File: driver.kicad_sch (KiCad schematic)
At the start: 39 parts, among them Q4 SIZ342ADT, Q5 SIZ342ADT, Q6 SIZ342ADT, U4 TMC6200

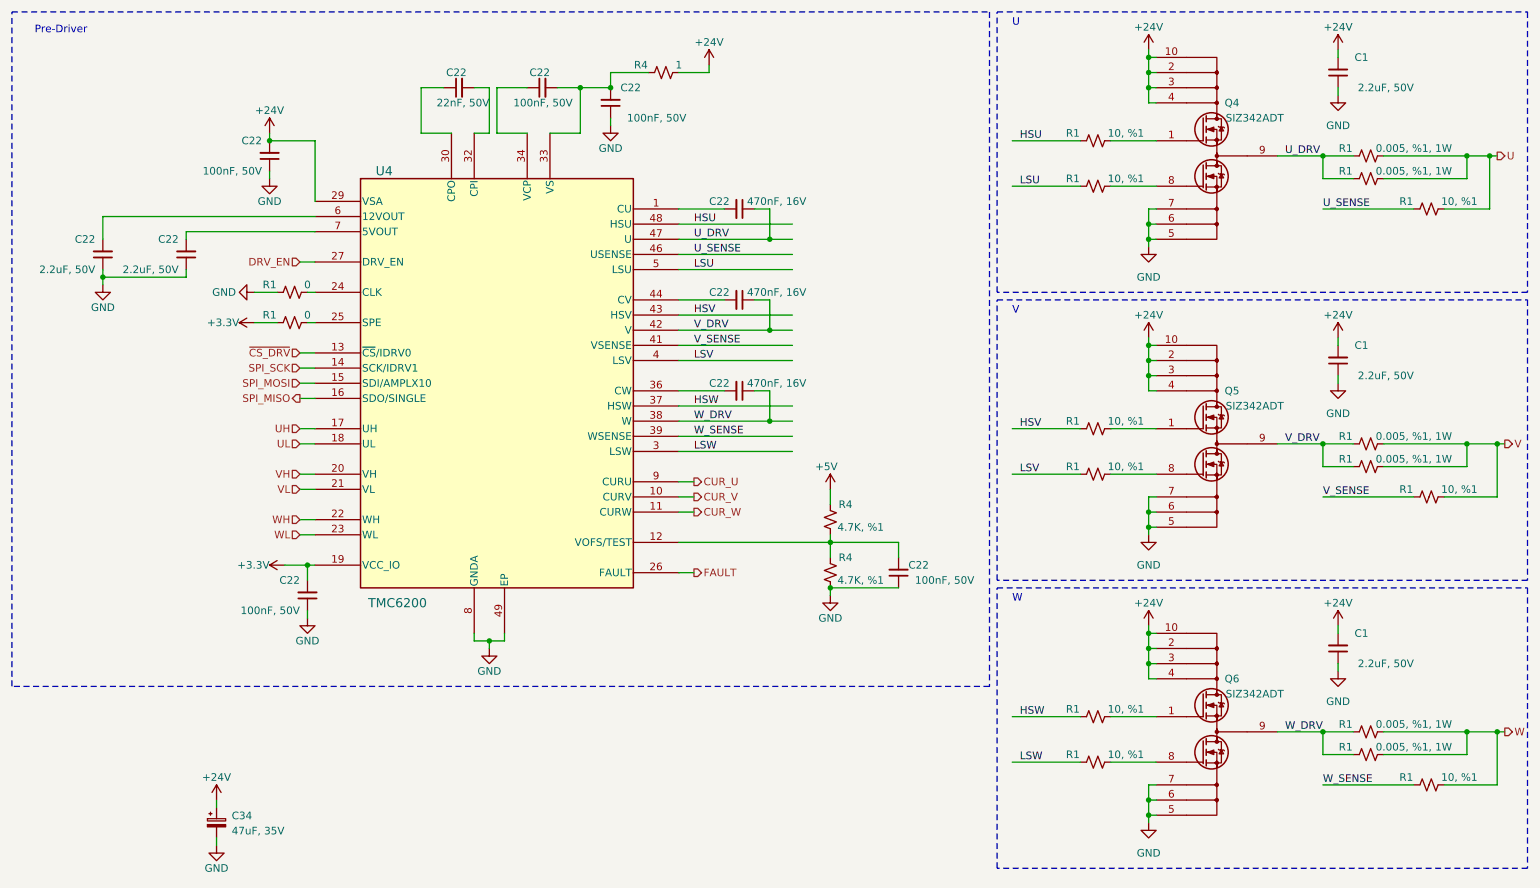
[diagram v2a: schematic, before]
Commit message: Optimize the BOM.
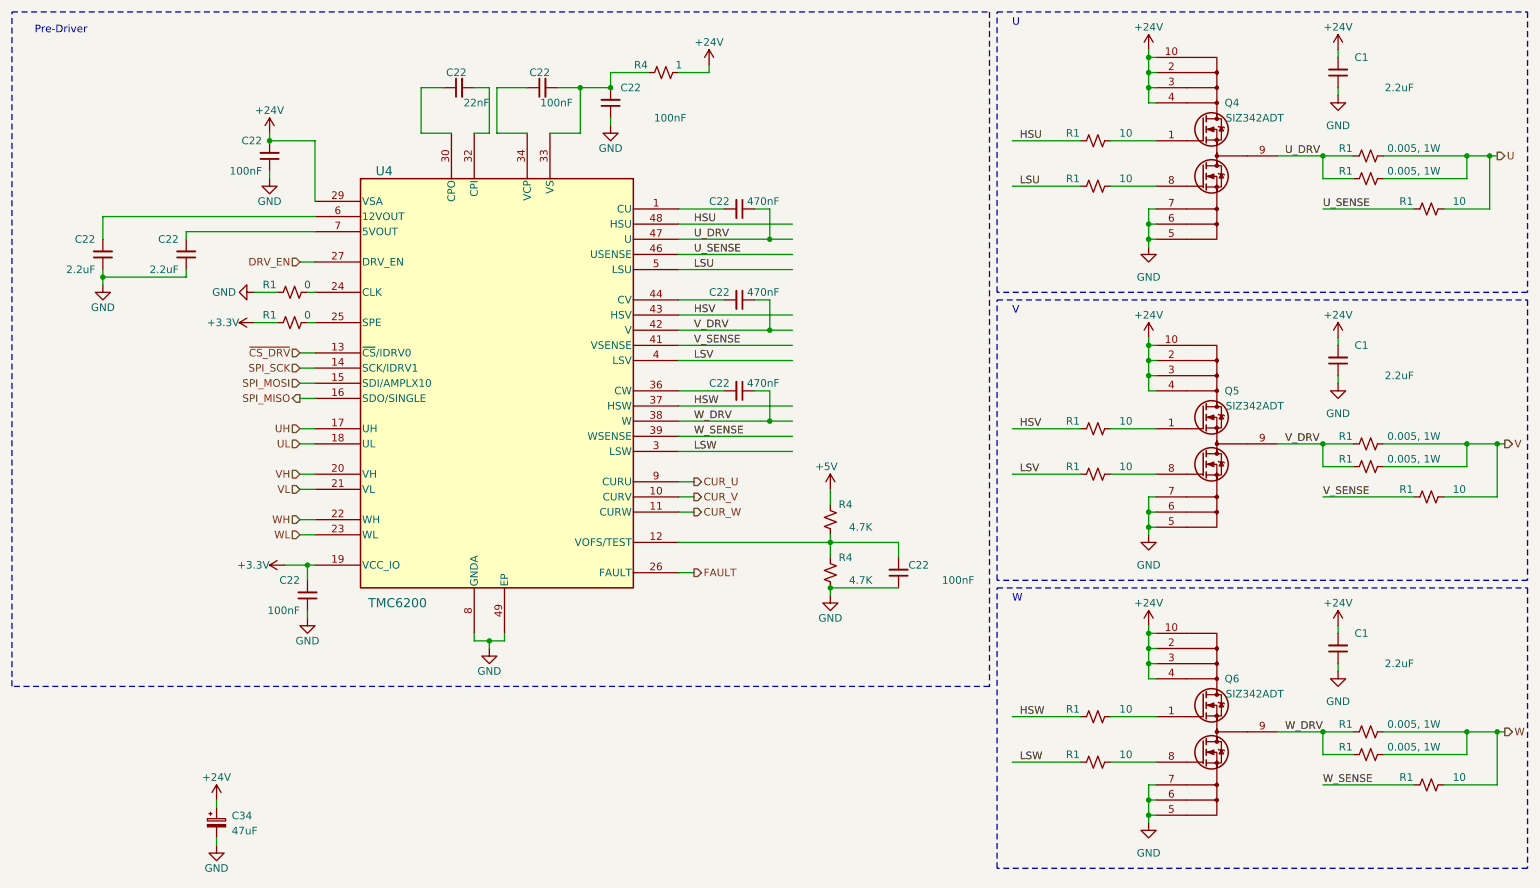
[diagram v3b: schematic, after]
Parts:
- C1, C22: value 2.2uF, 50V -> 2.2uF
- C22: value 100nF, 50V -> 100nF
- C22: value 22nF, 50V -> 22nF
- C22: value 470nF, 16V -> 470nF; MPN C0603C474K4RAC7867 -> GRM188R71E474KA12J
- C34: value 47uF, 35V -> 47uF
- R1: value 10, %1 -> 10
- R1: value 0.005, %1, 1W -> 0.005, 1W
- R4: value 4.7K, %1 -> 4.7K
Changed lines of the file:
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@@
       (effects (font (size 1.27 1.27)))
     )
-    (property "Value" "10, %1" (at 204.47 43.18 90)
+    (property "Value" "10" (at 204.47 43.18 90)
       (effects (font (size 1.27 1.27)))
     )
@@
       (effects (font (size 1.27 1.27)) (justify left))
     )
-    (property "Value" "100nF, 50V" (at 59.69 41.91 0)
+    (property "Value" "100nF" (at 59.69 41.91 0)
       (effects (font (size 1.27 1.27)) (justify left))
     )
@@
       (effects (font (size 1.27 1.27)) (justify left))
     )
-    (property "Value" "2.2uF, 50V" (at 31.75 58.42 0)
+    (property "Value" "2.2uF" (at 31.75 58.42 0)
       (effects (font (size 1.27 1.27)) (justify left))
     )
@@
       (effects (font (size 1.27 1.27)) (justify left))
     )
-    (property "Value" "100nF, 50V" (at 66.04 115.57 0)
+    (property "Value" "100nF" (at 66.04 115.57 0)
       (effects (font (size 1.27 1.27)) (justify left))
     )
@@
       (effects (font (size 1.27 1.27)) (justify left))
     )
-    (property "Value" "100nF, 50V" (at 111.76 30.48 90)
+    (property "Value" "100nF" (at 111.76 30.48 90)
       (effects (font (size 1.27 1.27)) (justify left))
     )
@@
       (effects (font (size 1.27 1.27)))
     )
-    (property "Value" "10, %1" (at 260.35 95.25 90)
+    (property "Value" "10" (at 260.35 95.25 90)
       (effects (font (size 1.27 1.27)))
     )
@@
       (effects (font (size 1.27 1.27)))
     )
-    (property "Value" "4.7K, %1" (at 160.02 101.6 0)
+    (property "Value" "4.7K" (at 160.02 101.6 0)
       (effects (font (size 1.27 1.27)))
     )
@@
       (effects (font (size 1.27 1.27)) (justify left))
     )
-    (property "Value" "100nF, 50V" (at 179.07 110.49 0)
+    (property "Value" "100nF" (at 179.07 110.49 0)
       (effects (font (size 1.27 1.27)) (justify left))
     )
@@
       (effects (font (size 1.27 1.27)))
     )
-    (property "Value" "0.005, %1, 1W" (at 252.73 138.43 90)
+    (property "Value" "0.005, 1W" (at 252.73 138.43 90)
       (effects (font (size 1.27 1.27)))
     )
@@
       (effects (font (size 1.27 1.27)) (justify left))
     )
-    (property "Value" "100nF, 50V" (at 130.81 33.02 0)
+    (property "Value" "100nF" (at 130.81 33.02 0)
       (effects (font (size 1.27 1.27)) (justify left))
     )
@@
       (effects (font (size 1.27 1.27)))
     )
-    (property "Value" "0.005, %1, 1W" (at 252.73 38.1 90)
+    (property "Value" "0.005, 1W" (at 252.73 38.1 90)
       (effects (font (size 1.27 1.27)))
     )
@@
       (effects (font (size 1.27 1.27)))
     )
-    (property "Value" "10, %1" (at 204.47 132.08 90)
+    (property "Value" "10" (at 204.47 132.08 90)
       (effects (font (size 1.27 1.27)))
     )
@@
       (effects (font (size 1.27 1.27)) (justify left))
     )
-    (property "Value" "47uF, 35V" (at 54.61 152.4889 0)
+    (property "Value" "47uF" (at 54.61 152.4889 0)
       (effects (font (size 1.27 1.27)) (justify left))
     )
@@
       (effects (font (size 1.27 1.27)))
     )
-    (property "Value" "0.005, %1, 1W" (at 252.73 41.91 90)
+    (property "Value" "0.005, 1W" (at 252.73 41.91 90)
       (effects (font (size 1.27 1.27)))
     )
@@
       (effects (font (size 1.27 1.27)))
     )
-    (property "Value" "10, %1" (at 204.47 83.82 90)
+    (property "Value" "10" (at 204.47 83.82 90)
       (effects (font (size 1.27 1.27)))
     )
@@
       (effects (font (size 1.27 1.27)) (justify left))
     )
-    (property "Value" "22nF, 50V" (at 97.79 30.48 90)
+    (property "Value" "22nF" (at 97.79 30.48 90)
       (effects (font (size 1.27 1.27)) (justify left))
     )
@@
       (effects (font (size 1.27 1.27)))
     )
-    (property "Value" "0.005, %1, 1W" (at 252.73 134.62 90)
+    (property "Value" "0.005, 1W" (at 252.73 134.62 90)
       (effects (font (size 1.27 1.27)))
     )
@@
       (effects (font (size 1.27 1.27)))
     )
-    (property "Value" "0.005, %1, 1W" (at 252.73 86.36 90)
+    (property "Value" "0.005, 1W" (at 252.73 86.36 90)
       (effects (font (size 1.27 1.27)))
     )
@@
       (effects (font (size 1.27 1.27)) (justify left))
     )
-    (property "Value" "2.2uF, 50V" (at 45.72 58.42 0)
+    (property "Value" "2.2uF" (at 45.72 58.42 0)
       (effects (font (size 1.27 1.27)) (justify left))
     )
@@
       (effects (font (size 1.27 1.27)) (justify left))
     )
-    (property "Value" "470nF, 16V" (at 140.97 77.47 90)
+    (property "Value" "470nF" (at 140.97 77.47 90)
       (effects (font (size 1.27 1.27)) (justify left))
     )
@@
       (effects (font (size 1.27 1.27)) hide)
     )
-    (property "MPN" "C0603C474K4RAC7867" (at 139.7 78.74 0)
+    (property "MPN" "GRM188R71E474KA12J" (at 139.7 78.74 0)
       (effects (font (size 1.27 1.27)) hide)
     )
@@
       (effects (font (size 1.27 1.27)) (justify left))
     )
-    (property "Value" "2.2uF, 50V" (at 252.73 27.94 0)
+    (property "Value" "2.2uF" (at 252.73 27.94 0)
       (effects (font (size 1.27 1.27)) (justify left))
     )
@@
       (effects (font (size 1.27 1.27)))
     )
-    (property "Value" "0.005, %1, 1W" (at 252.73 90.17 90)
+    (property "Value" "0.005, 1W" (at 252.73 90.17 90)
       (effects (font (size 1.27 1.27)))
     )
@@
       (effects (font (size 1.27 1.27)))
     )
-    (property "Value" "10, %1" (at 260.35 46.99 90)
+    (property "Value" "10" (at 260.35 46.99 90)
       (effects (font (size 1.27 1.27)))
     )
@@
       (effects (font (size 1.27 1.27)) (justify left))
     )
-    (property "Value" "470nF, 16V" (at 140.97 62.23 90)
+    (property "Value" "470nF" (at 140.97 62.23 90)
       (effects (font (size 1.27 1.27)) (justify left))
     )
@@
       (effects (font (size 1.27 1.27)) hide)
     )
-    (property "MPN" "C0603C474K4RAC7867" (at 139.7 63.5 0)
+    (property "MPN" "GRM188R71E474KA12J" (at 139.7 63.5 0)
       (effects (font (size 1.27 1.27)) hide)
     )
@@
       (effects (font (size 1.27 1.27)))
     )
-    (property "Value" "10, %1" (at 260.35 143.51 90)
+    (property "Value" "10" (at 260.35 143.51 90)
       (effects (font (size 1.27 1.27)))
     )
@@
       (effects (font (size 1.27 1.27)))
     )
-    (property "Value" "10, %1" (at 204.47 139.7 90)
+    (property "Value" "10" (at 204.47 139.7 90)
       (effects (font (size 1.27 1.27)))
     )
@@
       (effects (font (size 1.27 1.27)))
     )
-    (property "Value" "4.7K, %1" (at 160.02 110.49 0)
+    (property "Value" "4.7K" (at 160.02 110.49 0)
       (effects (font (size 1.27 1.27)))
     )
@@
       (effects (font (size 1.27 1.27)))
     )
-    (property "Value" "10, %1" (at 204.47 35.56 90)
+    (property "Value" "10" (at 204.47 35.56 90)
       (effects (font (size 1.27 1.27)))
     )
@@
       (effects (font (size 1.27 1.27)) (justify left))
     )
-    (property "Value" "2.2uF, 50V" (at 252.73 76.2 0)
+    (property "Value" "2.2uF" (at 252.73 76.2 0)
       (effects (font (size 1.27 1.27)) (justify left))
     )
@@
       (effects (font (size 1.27 1.27)))
     )
-    (property "Value" "10, %1" (at 204.47 91.44 90)
+    (property "Value" "10" (at 204.47 91.44 90)
       (effects (font (size 1.27 1.27)))
     )
@@
       (effects (font (size 1.27 1.27)) (justify left))
     )
-    (property "Value" "2.2uF, 50V" (at 252.73 124.46 0)
+    (property "Value" "2.2uF" (at 252.73 124.46 0)
       (effects (font (size 1.27 1.27)) (justify left))
     )
@@
       (effects (font (size 1.27 1.27)) (justify left))
     )
-    (property "Value" "470nF, 16V" (at 140.97 46.99 90)
+    (property "Value" "470nF" (at 140.97 46.99 90)
       (effects (font (size 1.27 1.27)) (justify left))
     )
@@
       (effects (font (size 1.27 1.27)) hide)
     )
-    (property "MPN" "C0603C474K4RAC7867" (at 139.7 48.26 0)
-      (effects (font (size 1.27 1.27)) hide)
-    )
+    (property "MPN" "GRM188R71E474KA12J" (at 139.7 48.26 0)
+      (effects (font (size 1.27 1.27)) hide)
+    )
